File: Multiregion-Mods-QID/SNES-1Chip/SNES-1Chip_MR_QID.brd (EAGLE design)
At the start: 88.9 x 40.6 mm, 42 parts, among them IC1 74HC27D, IC2 74HC30D

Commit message: Minor Updates: - Dual design for crystals (SNES-1Chip_MR_QID only); SMD and THT crystals are now supported (If THT crystals are used, SMD pads have to isolated, manually.) - minor tweaks of traces - EAGLE Version 7.5.0
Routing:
- net N$14: track 79.0 -> 76.7 mm
- net VCC: track 127.6 -> 129.7 mm
- net N$26: track 7.14 -> 5.34 mm
- net N$48: track 17.7 -> 17.0 mm
- net N$53: track 23.0 -> 23.7 mm
- net N$30: track 20.9 -> 21.5 mm, vias 0 -> 1
- net N$27: track 18.6 -> 18.8 mm, vias 0 -> 1
- net N$29: track 18.4 -> 18.6 mm, vias 0 -> 1
- net N$28: track 21.6 -> 21.5 mm, vias 0 -> 1
- net GND: vias 60 -> 59
- added copper zone on layer 16, net VCC
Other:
- board text added: "Rev:QID1.1"
- board text removed: "Rev:SE4.1"

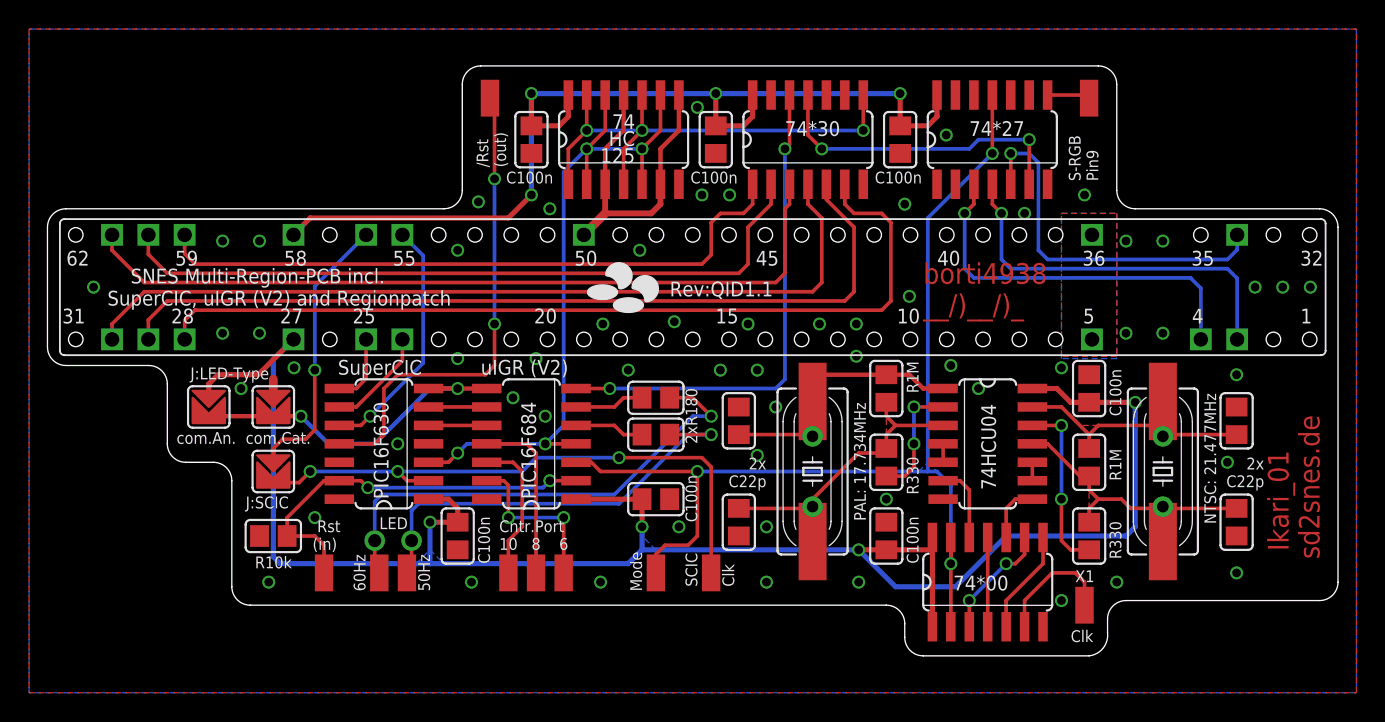
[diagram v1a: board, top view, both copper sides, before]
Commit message: add thermals to ground pad (easier to solder) and reduce PCB size a bit
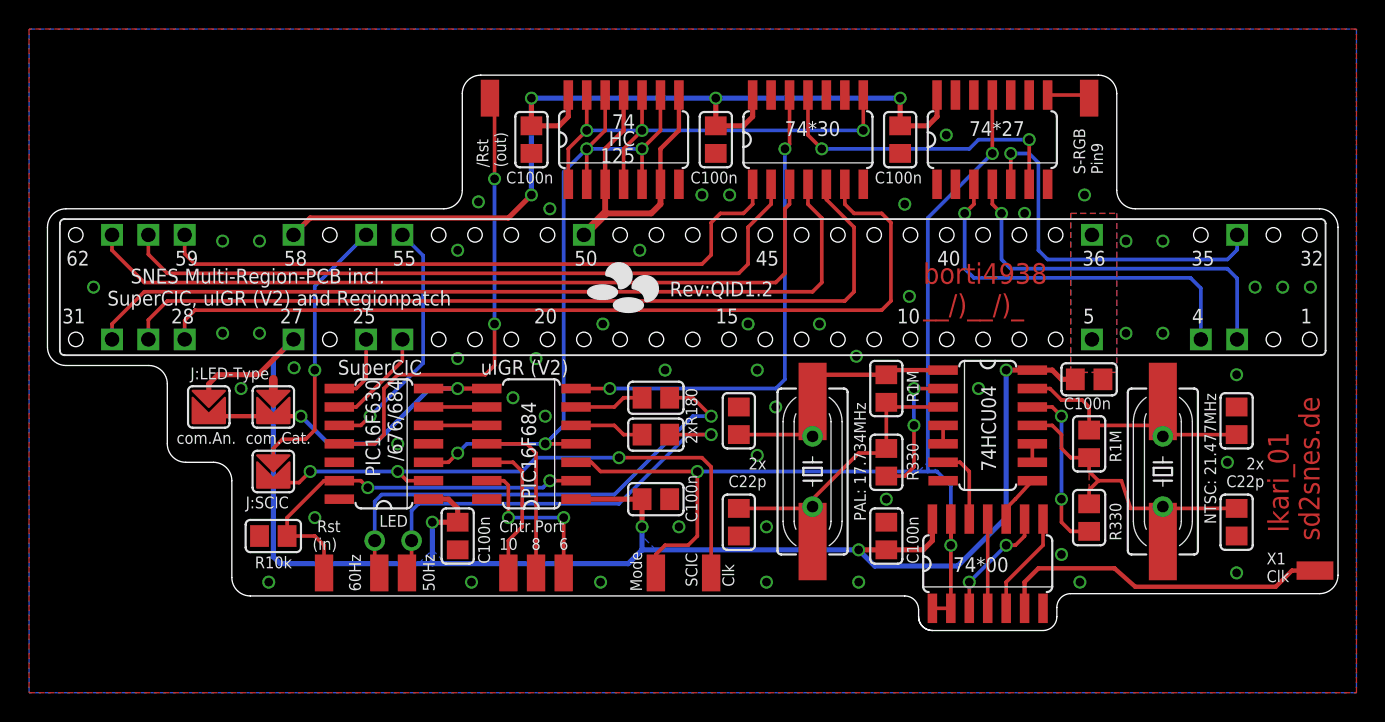
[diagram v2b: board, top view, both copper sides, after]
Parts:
- moved X1 16.1 mm to (88.6, 8.41), turned to 270 degrees
- moved 74*00 1.27 mm to (66.0, 8.89)
- moved 74HCU04 1.27 mm to (66.0, 18.4)
- moved R5 1.27 mm to (73.0, 12.1)
- moved R7 1.27 mm to (73.0, 17.1)
- moved C4 0.64 mm to (73.0, 21.6), turned to 0 degrees
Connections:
- net N$14: now also 74*00.1
- net VCC: no longer 74*00.1
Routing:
- net VCC: track 129.7 -> 114.7 mm
- net N$36: track 8.57 -> 23.1 mm
- net N$30: track 21.5 -> 23.2 mm
- net N$37: track 8.30 -> 9.57 mm
- net VCC_2: track 69.5 -> 68.2 mm
- net N$41: track 4.07 -> 3.36 mm
- net N$29: track 18.6 -> 19.1 mm
- net GND: vias 59 -> 53
- removed copper zone on layer 1, net N$28
- removed copper zone on layer 1, net N$29
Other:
- board size 88.9 x 40.6 mm -> 88.9 x 38.3 mm
- board text added: "PIC16F630 /676/684"
- board text added: "Rev:QID1.2"
- board text added: "X1 Clk"
- board text removed: "PIC16F630"
- board text removed: "Rev:QID1.1"
- board text removed: "X1"
